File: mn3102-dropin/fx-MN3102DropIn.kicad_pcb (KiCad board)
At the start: 2 copper layers, 6 parts, among them J1 MN3102_SOCKET, U1 CD4047B

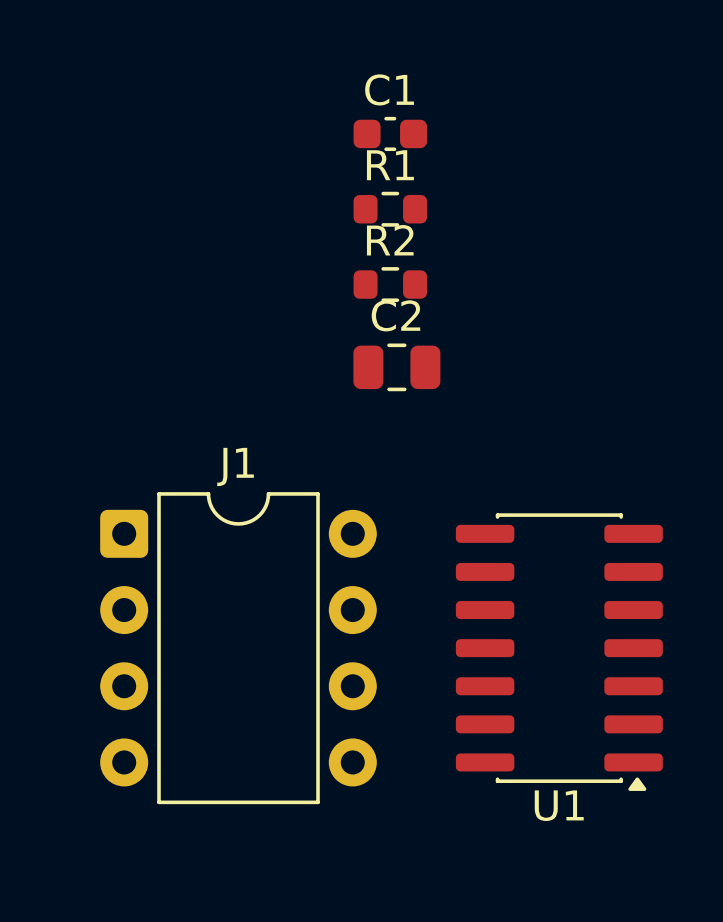
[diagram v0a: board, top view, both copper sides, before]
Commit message: mn3102-dropin: shrink C2 to optional 100n 0603; all-top layout guidance
VGG draws no DC current, so C2 is filtering insurance only (100nF corner
~1.7kHz vs 50-200kHz clock); many hosts already cap the VGG net
(PizzaPizza C21 22uF). Was 1u 0805 (up to 1.25mm tall) - now 100n 0603
C14663, same part as C1, and DNP-able.

README: recommend all-top construction (~12.7mm board, TSSOP center,
0603s on end tongues, bare bottom, ~2.5mm overhang) - overhang verified
clear against fx-PizzaPizza placement (nearest on-axis parts are 0.8mm
0603s flying ~3.5mm below); bottom-side alternate needs collared pins.
0402 Basic alternates listed.

Co-Authored-By: Claude Fable 5 <noreply@anthropic.com>
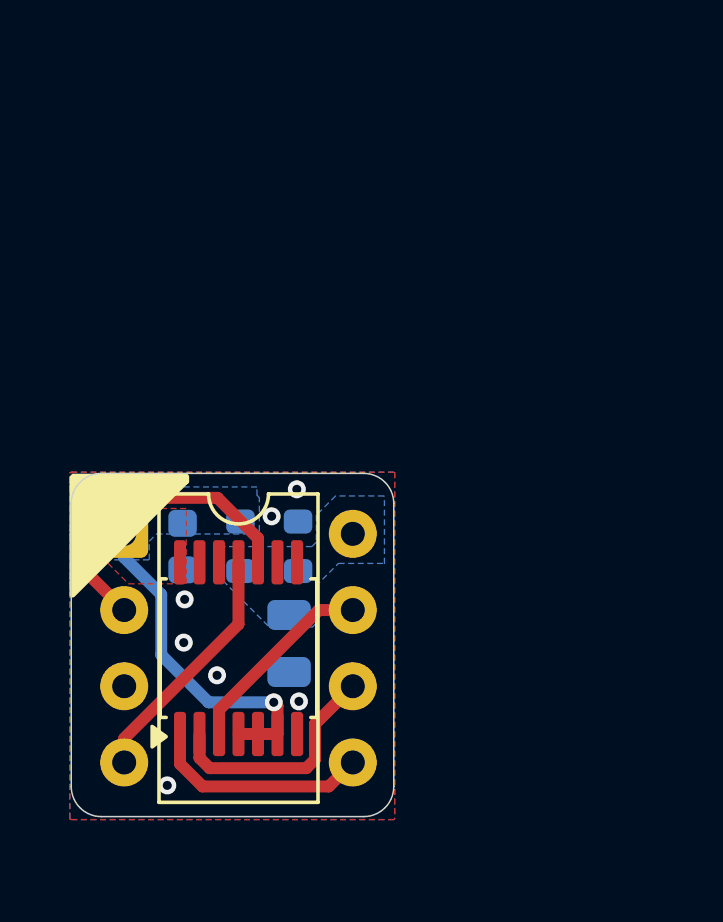
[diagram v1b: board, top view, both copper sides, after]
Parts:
- C1, C2, R1, R2: moved to B.Cu
- U1: footprint Package_SO:SOIC-14_3.9x8.7mm_P1.27mm -> Package_SO:TSSOP-14_4.4x5mm_P0.65mm
- moved C1 15.4 mm to (61.6, 47.8), turned to -90 degrees
- moved R1 12.3 mm to (63.5, 47.8), turned to -90 degrees
- moved U1 10.7 mm to (63.4, 51.2), turned to 90 degrees
- moved C2 9.88 mm to (65.1, 51.0), turned to -90 degrees
- moved R2 9.25 mm to (65.4, 47.8), turned to 90 degrees
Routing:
- net /VDD: track 0.00 -> 11.4 mm, vias 0 -> 1
- net /CP1: track 0.00 -> 11.0 mm
- net /CP2: track 0.00 -> 8.25 mm
- net /OX2: track 0.00 -> 7.87 mm
- net /OX3: track 0.00 -> 7.40 mm
- net /OX1: track 0.00 -> 6.64 mm
- net /GND: vias 0 -> 7
- added copper zone on B.Cu, net /GND
- added copper zone on F.Cu, net /GND
- added copper zone on B.Cu, net /VDD
- added copper zone on F.Cu, net /VDD
- added copper zone on B.Cu, net /VGG_OUT
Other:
- board outline added: 10.8 x 11.4 mm

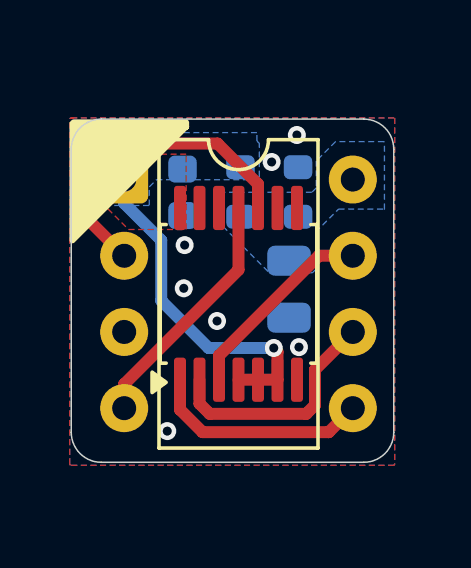
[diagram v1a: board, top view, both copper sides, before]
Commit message: mn3102-dropin: final adapter layout + JLC production files
Layout review passed: board netlist matches golden map, TSSOP-to-DIP pad
clearance measured 0.52mm, all parts top-side with bare bottom, solid
B.Cu GND pour with 17 stitching vias, DRC 0 unconnected (courtyard
overlap U1-in-J1 excluded by design, silk overlaps cosmetic).

Includes FABLOG entry from fab-hooks gerber generation.

Co-Authored-By: Claude Fable 5 <noreply@anthropic.com>
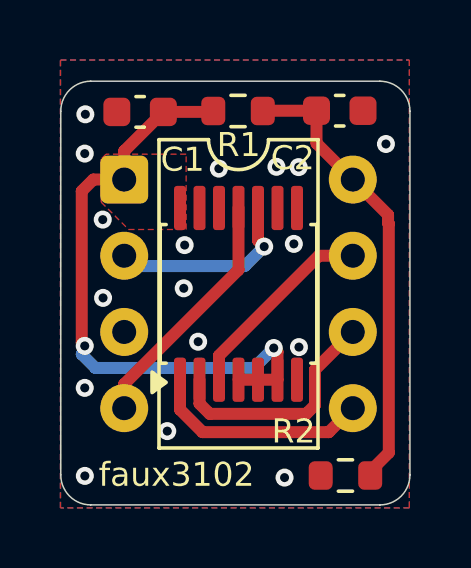
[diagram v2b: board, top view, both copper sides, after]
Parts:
- C1, R1, R2: moved to F.Cu
- C2: value 1u -> 100n; footprint Capacitor_SMD:C_0805_2012Metric -> Capacitor_SMD:C_0603_1608Metric; moved to F.Cu
- moved R2 9.58 mm to (67.0, 57.2), turned to 180 degrees
- moved C2 6.19 mm to (66.8, 45.1), turned to 0 degrees
- moved C1 3.03 mm to (60.2, 45.1), turned to 180 degrees
- moved R1 2.70 mm to (63.4, 45.1), turned to 0 degrees
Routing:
- net /VGG_OUT: track 0.00 -> 15.2 mm
- net /VDD: track 11.4 -> 20.9 mm, vias 1 -> 2
- net /CP1: track 11.0 -> 6.45 mm, vias 0 -> 1
- net /GND: vias 7 -> 17
- removed copper zone on B.Cu, net /VDD
- removed copper zone on B.Cu, net /VGG_OUT
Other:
- board size 10.8 x 11.4 mm -> 11.6 x 14.1 mm
- board text added: "${REVISION}"
- board text added: "faux3102"
